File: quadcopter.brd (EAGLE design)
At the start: 137.4 x 137.4 mm, 73 parts, among them J1 AVR_SPI_PRG_6NS, U3 ATMEGA128RFA1

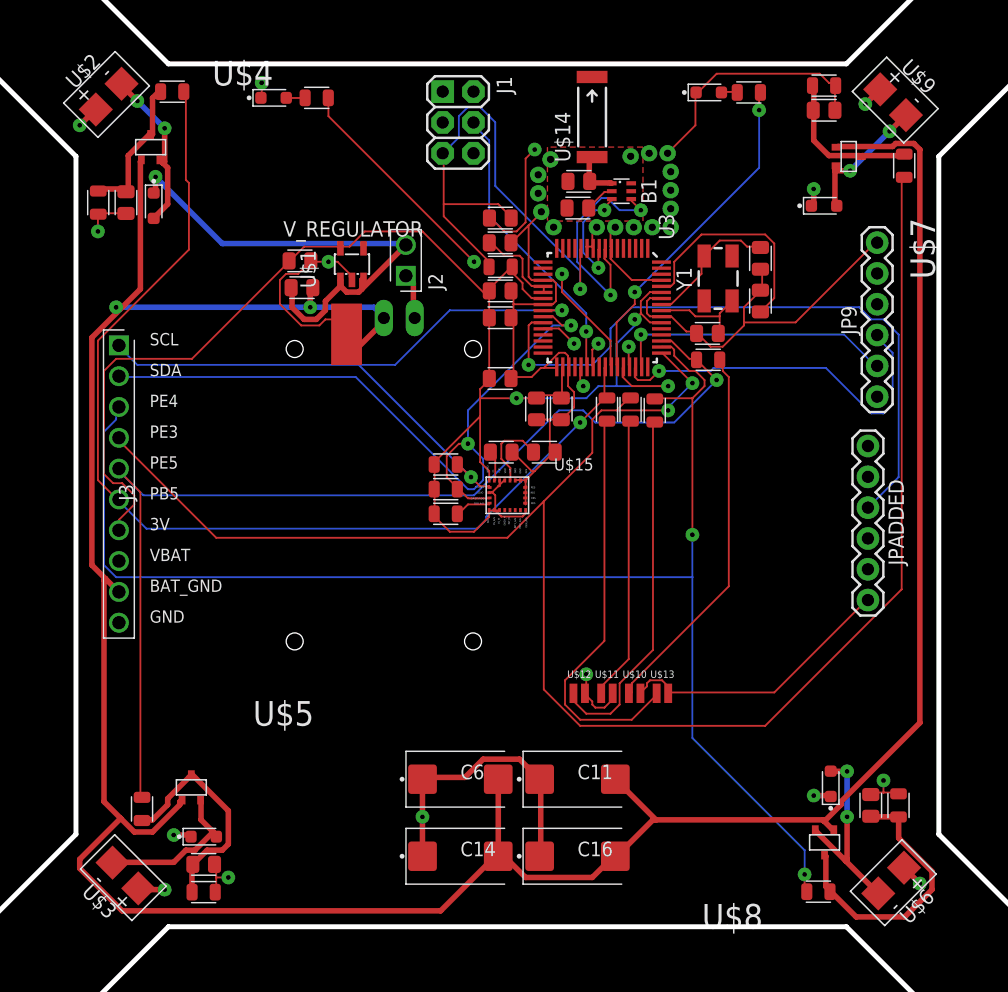
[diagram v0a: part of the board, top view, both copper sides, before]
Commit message: fixed crystal routing and antenna routing, moved motor recouping caps, and replaced wrong filter diodes
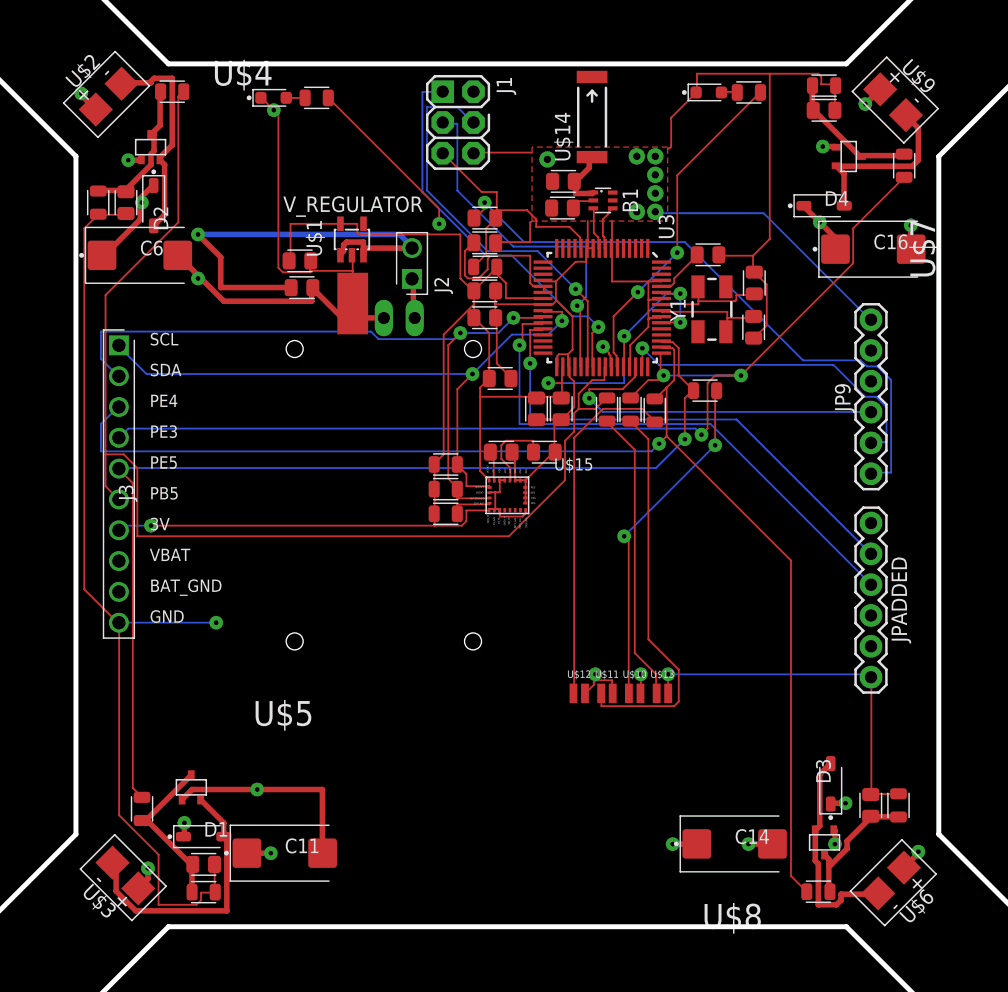
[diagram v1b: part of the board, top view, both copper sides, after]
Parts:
- D1, D2, D3, D4: value 20V-500MA -> 360mV; device quadparts_prebuilt:LEDSC125X200X120-2_HS -> quadparts_prebuilt:SOD3716X135_HS
- moved C16 55.7 mm to (30.2, 20.3)
- moved C6 50.6 mm to (-30.3, 19.8)
- moved C11 24.9 mm to (-18.4, -29.5)
- moved C14 22.6 mm to (18.7, -28.7)
- moved JP9 6.37 mm to (30.0, 1.78)
- moved JPADDED 6.36 mm to (30.0, -2.29)
- moved C19 5.76 mm to (16.5, 19.8), turned to 0 degrees
- moved C9 3.84 mm to (20.3, 13.9), turned to 270 degrees
- moved U$1 2.59 mm to (-12.7, 17.1)
- moved Y1 2.59 mm to (16.9, 15.3)
- moved R1 2.55 mm to (16.3, 8.63)
- moved C12 2.09 mm to (20.4, 17.5), turned to 90 degrees
- moved V_REGULATOR 2.03 mm to (-12.8, 21.1)
- moved B1 1.70 mm to (7.88, 24.3)
- moved C5 1.27 mm to (4.54, 23.7)
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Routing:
- net BAT_GND: track 245.5 -> 45.7 mm, vias 2 -> 7
- net GND: track 170.4 -> 286.9 mm, vias 23 -> 12
- net PE3: track 148.0 -> 89.9 mm, vias 2 -> 3
- net RESET: track 44.5 -> 22.5 mm, vias 1 -> 0
- net RFP: track 18.9 -> 3.75 mm, vias 2 -> 0
- net AVDD: track 18.5 -> 4.26 mm
- net PE4: track 117.2 -> 103.7 mm, vias 2 -> 1
- net VCC: track 77.0 -> 63.7 mm, vias 9 -> 11
- net FILTEREDNE: track 22.8 -> 11.1 mm
- net PB5: track 86.3 -> 96.7 mm, vias 1 -> 0
- net N$11: track 33.9 -> 24.1 mm
- net MOSI: track 24.0 -> 33.7 mm
- net RX1: track 54.1 -> 44.6 mm
- net TX1: track 31.9 -> 41.2 mm
- net FLYBACKSW: track 13.3 -> 22.3 mm
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- added copper zone on layer 15, net BAT_GND

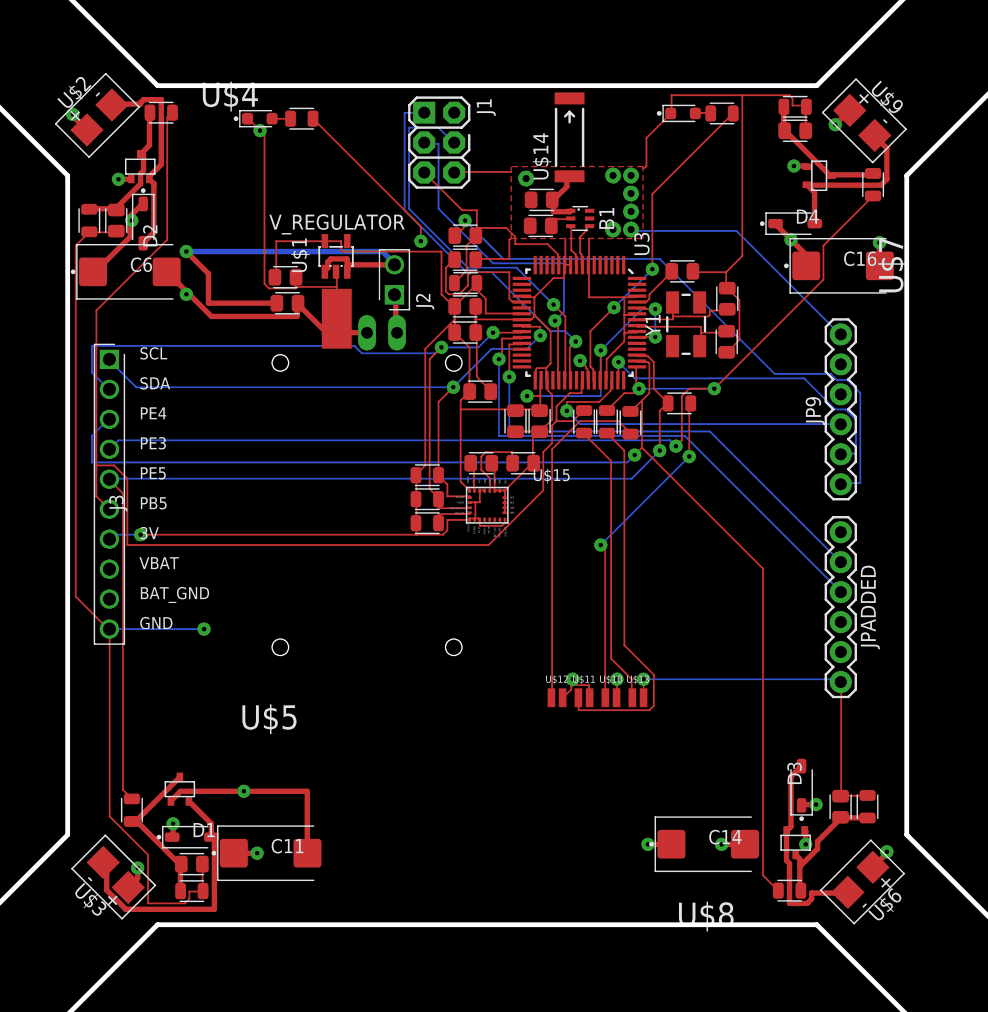
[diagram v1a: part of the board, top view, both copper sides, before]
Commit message: fixed mosfet padding, rerouted, added gerber files
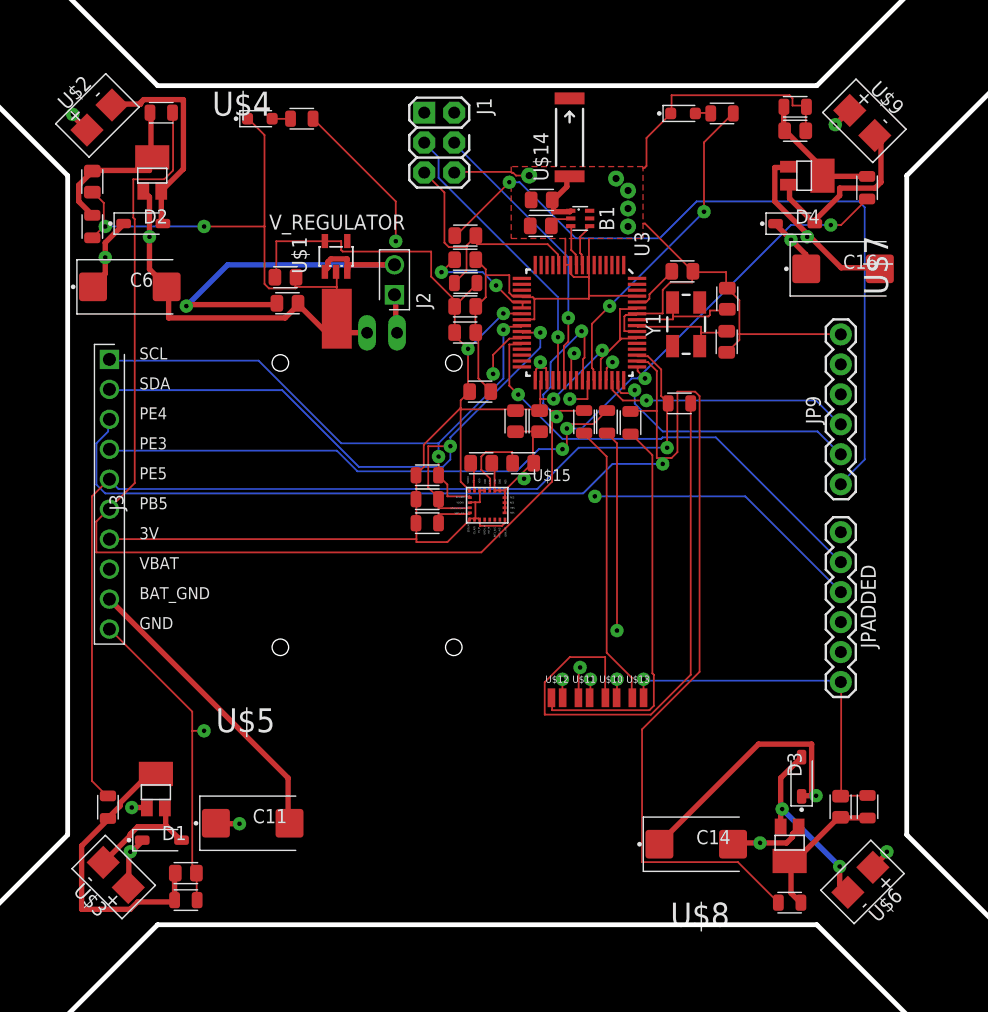
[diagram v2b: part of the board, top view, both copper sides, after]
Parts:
- moved C10 3.88 mm to (-33.5, 27.4)
- moved C11 2.96 mm to (-19.9, -27.0)
- moved D1 2.55 mm to (-27.6, -28.4)
- moved R2 2.05 mm to (-32.1, -25.6)
- moved U$5 2.05 mm to (-28.1, -24.3)
- moved C6 1.27 mm to (-30.3, 18.5)
- moved U$7 1.27 mm to (26.9, 27.9)
- moved U$4 1.27 mm to (-28.4, 27.9)
- moved C14 1.02 mm to (17.7, -28.7)
- moved R6 1.02 mm to (25.6, -33.7)
- moved C13 0.92 mm to (-25.5, -31.2)
- moved R5 0.92 mm to (-25.5, -33.5)
- moved D3 0.76 mm to (26.6, -23.0)
- moved R4 0.57 mm to (-33.5, 23.6)
- moved R13 0.57 mm to (32.2, 26.9)
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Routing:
- net GND: track 286.9 -> 229.8 mm, vias 12 -> 15
- net BAT_GND: track 45.7 -> 78.8 mm, vias 7 -> 4
- net PE4: track 103.7 -> 131.1 mm
- net N$2: track 28.3 -> 49.0 mm, vias 2 -> 0
- net VCC: track 63.7 -> 81.0 mm, vias 11 -> 9
- net 3V: track 142.9 -> 126.9 mm, vias 5 -> 4
- net N$21: track 50.6 -> 64.4 mm
- net FLYBACKSW: track 22.3 -> 10.1 mm
- net FILTEREDSW: track 13.6 -> 24.9 mm
- net MOSI: track 33.7 -> 24.3 mm
- net PB5: track 96.7 -> 105.3 mm, vias 0 -> 2
- net PE3: track 89.9 -> 81.5 mm, vias 3 -> 4
- net N$5: track 32.3 -> 24.1 mm, vias 0 -> 2
- net RX0: track 29.5 -> 21.4 mm
- net TX0: track 27.9 -> 23.0 mm
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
